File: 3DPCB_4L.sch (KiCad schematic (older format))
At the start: 196 parts, among them IC1 A5984_LP, IC2 A5984_LP, IC3 A5984_LP, IC4 A5984_LP, IC5 A5984_LP, IC6 MP9943, J10 , J11 , J12 , J13 , J14 , J15 , J16 , J5 , J6 , J7 , J8 , J9 , K1 CONN_3, K2 CONN_3, K3 CONN_3, K4 CONN_3, K5 CONN_3, K6 CONN_3, K7 CONN_3, K8 CONN_3, K9 CONN_3, P1 CONN_8, P11 CONN_3X2, P12 CONN_3X2, P13 CONN_4, P2 CONN_8, P5 CONN_4, P6 CONN_4, P7 CONN_4, P8 CONN_02X03, P9 CONN_4, U1 CONN_4_LERCHE, U10 MICRO-SD, U11 TC4427, U12 MCP4728, U13 CONN_4_LERCHE, U15 SPST_MOMENTARY, U16 CONN_4_LERCHE, U2 SPST_MOMENTARY, U21 CONN_4_LERCHE, U22 CONN_4_LERCHE, U23 MCP4728, U24 IRFH5302, U25 CONN_4_LERCHE, U3 BSS84, U4 CONN_4_LERCHE, U5 IRFH5302, U6 LPC1768_TQFP100, U7 IRFH5302, U8 IRFH5302, U9 TC4427

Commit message: Starting the work
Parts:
- removed C17: 100n, LercheTech:Lerche_C0603, symbol C-RESCUE-3DPCB_4L
- removed C9: 18p, LercheTech:Lerche_C0603, symbol C-RESCUE-3DPCB_4L
- removed D6: LED, LEDs:LED_0603, symbol LED-RESCUE-3DPCB_4L
- removed J10, J11, J12, J13, J14, J15, J16, J5, J6, J7, J8, J9: (no value), LercheTech:Lerche_2PsolderJumper, symbol SOLDER_JUMPER
- removed K8: CONN_3, Pin_Headers:Pin_Header_Straight_1x03, symbol CONN_3
- removed L1: INDUCTOR, LercheTech:Lerche_R0603, symbol INDUCTOR
- removed P11: CONN_3X2, Pin_Headers:Pin_Header_Straight_2x03, symbol CONN_3X2
- removed P12: CONN_3X2, LercheTech:Lerche_6P_1.6mm_2ROW, symbol CONN_3X2
- removed R28: 1k, LercheTech:Lerche_R0603, symbol R-RESCUE-3DPCB_4L
- removed R9: 10k, LercheTech:Lerche_R0603, symbol R-RESCUE-3DPCB_4L
- removed U10: MICRO-SD, LercheTech:Lerche_Molex_502774-0891, symbol MICRO-SD
- removed U15: SPST_MOMENTARY, LercheTech:Lerche_SPST_ITEAD, symbol SPST_MOMENTARY
- removed U16: CONN_4_LERCHE, LercheTech:Lerche_4P_2.54mm, symbol CONN_4_LERCHE
- removed U3: BSS84, LercheTech:Lerche_SOT23-3, symbol BSS84
- removed U6: LPC1768_TQFP100, Housings_QFP:TQFP-100_14x14mm_Pitch0.5mm, symbol LPC1768_TQFP100
- added C9: 1uF, LercheTech:Lerche_C0603, symbol C
- added L3, L4: L_Small, Resistors_SMD:R_0603, symbol L_Small
- added U10: MICRO-SD_Molex_502774-0891, LercheTech:Lerche_Molex_502774-0891, symbol MICRO-SD_Molex_502774-0891
- added U3: CONN_4_LERCHE, LercheTech:Lerche_4P_2.54mm, symbol CONN_4_LERCHE
- C5: value 18p -> 100n
- IC7: renamed from IC?; footprint (none) -> LercheTech:TFBGA180
- JP1, JP2: renamed from JP?; footprint (none) -> Pin_Headers:Pin_Header_Straight_1x03_Pitch2.54mm
- L5, L6, L7, L8: renamed from L?; footprint (none) -> Resistors_SMD:R_0603
- P8: footprint (none) -> LercheTech:Lerche_2x3P_3.5mm_Molex_UltraFit
- R11: value 1k5 -> 12k1 1%
- R42, R43: value 10k -> 4K7
- R44, R45: value 3k3 -> 4K7
- R7: value 33R -> 100R
- R8: value 33R -> 10k
- gave numbers to parts that had none: 5
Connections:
- net DAC_SCL is gone; now on net ISC0_SCL: R19.1, U12.2 (SCL), U23.2 (SCL)
- net DAC_SDA is gone; now on net ISC0_SDA: R18.1, U12.3 (SDA), U23.3 (SDA)
- net LED1 is gone; now on net MCU_G2_10: R3.2, U4.1
- net LED2 is gone; now on net MCU_G2_9: R4.2, U4.2
- net M1_MS1 is gone; now on net MCU_G1_13: IC1.5 (MS1)
- net P2.4 is gone; now on net MCU_PWM15: U9.2 (IN)
- net P2.5 is gone; now on net MCU_PWM14: U9.4 (IN)
- net P2.6 is gone; now on net MCU_PWM13: U11.2 (IN)
- net P2.7 is gone; now on net MCU_PWM12: U11.4 (IN)
- net PLAY is gone; now on net MCU_~ISP: R27.2
- net RX_0 is gone; now on net MCU_RXD0: K7.2 (PM)
- net SD_MOSI is gone; now on net +3.3V: R41.2
- net TH1 is gone; now on an unnamed net: C3.1, P1.2 (P2), R34.2
- net TH2 is gone; now on an unnamed net: C4.1, P1.4 (P4), R10.2
- net TH3 is gone; now on an unnamed net: C7.1, P1.6 (P6), R12.2
- net TH4 is gone; now on an unnamed net: C10.1, P1.8 (P8), R13.2
- net TX_0 is gone; now on net MCU_TXD0: K7.1 (P1)
- net USB_D- is gone; now on net USB0_VBUS: R7.2
- net X-MAX is gone; now on net MCU_G2_0: K2.3 (P3)
- net X-MIN is gone; now on net MCU_G4_0: K1.3 (P3)
- net +3.3V: now also C5.1, IC7.B9 (VBAT), IC7.D8 (VDDREG), IC7.E8 (VDDREG), IC7.G10 (VDDIO), IC7.H10 (VDDIO), IC7.H5 (VDDIO), IC7.K8 (VDDIO), R8.1, C9.1, U10.4 (+3V3); no longer IC7.B9 (VBAT), IC7.D8 (VDDREG), IC7.E8 (VDDREG), IC7.G10 (VDDIO), IC7.H10 (VDDIO), IC7.H5 (VDDIO), IC7.K8 (VDDIO), R41.1, R42.1, R43.1, R44.1, R45.1
- net ADC0/DAC: now also IC7.B6 (ADC0/DAC); no longer IC7.B6 (ADC0/DAC)
- net ADC1: now also IC7.C4 (ADC1), R42.1; no longer IC7.C4 (ADC1)
- net ADC2: now also IC7.B3 (ADC2), R43.1; no longer IC7.B3 (ADC2)
- net ADC3: now also IC7.B4 (ADC3), R44.1; no longer IC7.B4 (ADC3)
- net ADC4: now also IC7.A5 (ADC4), R45.1; no longer IC7.A5 (ADC4)
- net ADC5: now also IC7.C3 (ADC5); no longer IC7.C3 (ADC5)
- net ADC6: now also IC7.A4 (ADC6); no longer IC7.A4 (ADC6)
- net ADC7: now also IC7.B5 (ADC7); no longer IC7.B5 (ADC7)
- net DBGEN: now also IC7.K4 (DBGEN); no longer IC7.K4 (DBGEN)
- net DRV_RESET: now also IC7.H13 (P6_9)
- net FPGA_PROG: now also IC7.K1 (P8_8); no longer IC7.K1 (P8_8)
- net GND: now also IC7.D7 (VSS), IC7.E6 (VSS), IC7.E7 (VSS), IC7.E9 (VSS), IC7.F10 (VSS), IC7.K6 (VSS), IC7.K9 (VSS), R11.2, C9.2, L4.1, U10.10 (CardDetect), U10.11 (Shield), U10.12 (Shield), U10.13 (Shield), U10.14 (Shield), U10.6 (GND), U3.4; no longer IC7.D7 (VSS), IC7.E6 (VSS), IC7.E7 (VSS), IC7.E9 (VSS), IC7.F10 (VSS), IC7.K6 (VSS), IC7.K9 (VSS)
- net ISC0_SCL: now also IC7.K13 (ISC0_SCL); no longer IC7.K13 (ISC0_SCL)
- net ISC0_SDA: now also IC7.K14 (ISC0_SDA); no longer IC7.K14 (ISC0_SDA)
- net MCU_ADC6: now also IC7.C5 (PB_6); no longer IC7.C5 (PB_6)
- net MCU_BOOT0: now also IC7.N1 (P1_1); no longer IC7.N1 (P1_1)
- net MCU_BOOT1: now also IC7.N2 (P1_2); no longer IC7.N2 (P1_2)
- net MCU_BOOT2: now also IC7.H14 (P2_8); no longer IC7.H14 (P2_8)
- net MCU_BOOT3: now also IC7.G14 (P2_9); no longer IC7.G14 (P2_9)
- net MCU_G0_5: now also IC3.11 (STEP), IC7.K12 (P6_6); no longer IC7.K12 (P6_6)
- net MCU_G1_0: now also IC7.N4 (P1_7); no longer IC7.N4 (P1_7)
- net MCU_G1_1: now also IC7.M5 (P1_8); no longer IC7.M5 (P1_8)
- net MCU_G1_11: now also IC2.5 (MS1), IC7.E13 (P2_11); no longer IC7.E13 (P2_11)
- net MCU_G1_12: now also IC2.23 (~ENABLE), IC7.D13 (P2_12); no longer IC7.D13 (P2_12)
- net MCU_G1_13: now also IC7.E14 (P2_13); no longer IC7.E14 (P2_13)
- net MCU_G2_0: now also IC7.D4 (P4_0); no longer IC7.D4 (P4_0)
- net MCU_G2_10: now also IC7.M1 (P5_1); no longer IC7.M1 (P5_1)
- net MCU_G2_11: now also IC7.M3 (P5_2); no longer IC7.M3 (P5_2)
- net MCU_G2_12: now also IC7.P6 (P5_3); no longer IC7.P6 (P5_3)
- net MCU_G2_13: now also IC7.N7 (P5_4); no longer IC7.N7 (P5_4)
- net MCU_G2_14: now also IC7.N8 (P5_5); no longer IC7.N8 (P5_5)
- net MCU_G2_15: now also IC7.M11 (P5_6); no longer IC7.M11 (P5_6)
- net MCU_G2_4: now also IC7.A1 (P4_4); no longer IC7.A1 (P4_4)
- net MCU_G2_7: now also IC7.N11 (P5_7); no longer IC7.N11 (P5_7)
- net MCU_G2_9: now also IC7.L2 (P5_0); no longer IC7.L2 (P5_0)
- net MCU_G3_0: now also IC4.11 (STEP), IC7.P14 (P6_1); no longer IC7.P14 (P6_1)
- net MCU_G3_1: now also IC3.10 (MS3), IC7.K11 (P6_2); no longer IC7.K11 (P6_2)
- net MCU_G3_10: now also IC1.23 (~ENABLE), IC7.A14 (P7_2); no longer IC7.A14 (P7_2)
- net MCU_G3_2: now also IC4.6 (MS2), IC7.N13 (P6_3); no longer IC7.N13 (P6_3)
- net MCU_G3_3: now also IC4.14 (DIR), IC7.M14 (P6_4); no longer IC7.M14 (P6_4)
- net MCU_G3_4: now also IC4.10 (MS3), IC7.L14 (P6_5); no longer IC7.L14 (P6_5)
- net MCU_G3_5: no longer IC7.H13 (P6_9)
- net MCU_G3_6: now also IC2.11 (STEP), IC7.G13 (P6_10); no longer IC7.G13 (P6_10)
- net MCU_G4_0: now also IC7.E4 (P8_0); no longer IC7.E4 (P8_0)
- net MCU_G5_12: now also IC7.D2 (P4_8); no longer IC7.D2 (P4_8)
- net MCU_G5_15: now also IC2.14 (DIR), IC7.H11 (P6_7); no longer IC7.H11 (P6_7)
- net MCU_G5_6: now also IC3.6 (MS2), IC7.J14 (P2_6); no longer IC7.J14 (P2_6)
- net MCU_G6_25: now also IC7.M7 (PD_11); no longer IC7.M7 (PD_11)
- net MCU_G6_26: now also IC7.P9 (PD_12); no longer IC7.P9 (PD_12)
- net MCU_G6_28: now also IC7.L11 (PD_14); no longer IC7.L11 (PD_14)
- net MCU_G6_29: now also IC7.P13 (PD_15); no longer IC7.P13 (PD_15)
- net MCU_G6_30: now also IC7.P12 (PD_16); no longer IC7.P12 (PD_16)
- net MCU_G7_2: now also IC3.14 (DIR), IC7.L12 (PE_2); no longer IC7.L12 (PE_2)
- net MCU_G7_3: now also IC3.23 (~ENABLE), IC7.K10 (PE_3); no longer IC7.K10 (PE_3)
- net MCU_G7_4: now also IC3.5 (MS1), IC7.J11 (PE_4); no longer IC7.J11 (PE_4)
- net MCU_MISO1: now also IC7.M2 (P1_3); no longer IC7.M2 (P1_3)
- net MCU_MOSI1: now also IC7.P2 (P1_4); no longer IC7.P2 (P1_4)
- net MCU_PWM0: now also IC7.A2 (P4_2); no longer IC7.A2 (P4_2)
- net MCU_PWM1: now also IC7.D3 (P4_1); no longer IC7.D3 (P4_1)
- net MCU_PWM10: now also IC7.D14 (PB_0); no longer IC7.D14 (PB_0)
- net MCU_PWM11: now also IC7.F5 (P7_6); no longer IC7.F5 (P7_6)
- net MCU_PWM12: now also IC7.A7 (P7_5); no longer IC7.A7 (P7_5)
- net MCU_PWM13: now also IC7.C6 (P7_4); no longer IC7.C6 (P7_4)
- net MCU_PWM14: now also IC7.B14 (P7_0); no longer IC7.B14 (P7_0)
- net MCU_PWM15: now also IC7.C13 (P7_1); no longer IC7.C13 (P7_1)
- net MCU_PWM2: now also IC7.F14 (P2_10); no longer IC7.F14 (P2_10)
- net MCU_PWM3: now also IC7.B2 (P4_3); no longer IC7.B2 (P4_3)
- net MCU_PWM4: now also IC7.B1 (P4_6); no longer IC7.B1 (P4_6)
- net MCU_PWM5: now also IC7.C2 (P4_5); no longer IC7.C2 (P4_5)
- net MCU_PWM6: now also IC7.A13 (PB_1); no longer IC7.A13 (PB_1)
- net MCU_PWM7: now also IC7.B11 (PB_2); no longer IC7.B11 (PB_2)
- net MCU_PWM8: now also IC7.A12 (PB_3); no longer IC7.A12 (PB_3)
- net MCU_PWM9: now also IC7.E12 (PA_4); no longer IC7.E12 (PA_4)
- net MCU_RD0: now also IC7.D10 (P3_1); no longer IC7.D10 (P3_1)
- net MCU_RD1: now also IC7.M12 (PE_1); no longer IC7.M12 (PE_1)
- net MCU_RXD0: now also IC7.M13 (P2_1); no longer IC7.M13 (P2_1)
- net MCU_RXD1: now also IC7.K7 (P1_14); no longer IC7.K7 (P1_14)
- net MCU_RXD2: now also IC7.J13 (PA_2); no longer IC7.J13 (PA_2)
- net MCU_RXD3: now also IC7.L9 (P2_4); no longer IC7.L9 (P2_4)
- net MCU_SCK0: now also IC7.D12 (P3_0); no longer IC7.D12 (P3_0)
- net MCU_SCK1: now also IC7.D6 (PF_4); no longer IC7.D6 (PF_4)
- net MCU_SGPIO0: now also IC7.P1 (P9_0); no longer IC7.P1 (P9_0)
- net MCU_SGPIO15: now also IC7.L3 (P4_10); no longer IC7.L3 (P4_10)
- net MCU_SSEL1: now also IC7.N3 (P1_5); no longer IC7.N3 (P1_5)
- net MCU_TD0: now also IC7.D9 (P3_2); no longer IC7.D9 (P3_2)
- net MCU_TD1: now also IC7.N12 (PE_0); no longer IC7.N12 (PE_0)
- net MCU_TXD0: now also IC7.N14 (P2_0); no longer IC7.N14 (P2_0)
- net MCU_TXD2: now also IC7.H12 (PA_1); no longer IC7.H12 (PA_1)
- net MCU_TXD3: now also IC7.G11 (P2_3); no longer IC7.G11 (P2_3)
- net MCU_~DFU: now also IC7.J2 (P4_9), R8.2, U3.1; no longer IC7.J2 (P4_9)
- net MCU_~ISP: now also IC7.G12 (P2_7), U3.2; no longer IC7.G12 (P2_7)
- net NC_CGU1: now also IC7.L10 (PA_0); no longer IC7.L10 (PA_0)
- net NC_ETH_CRS: now also IC7.L5 (P1_16); no longer IC7.L5 (P1_16)
- net NC_ETH_LED1: now also IC7.L1 (P1_0); no longer IC7.L1 (P1_0)
- net NC_ETH_MDC: now also IC7.D5 (P7_7); no longer IC7.D5 (P7_7)
- net NC_ETH_MDIO: now also IC7.L6 (P1_17); no longer IC7.L6 (P1_17)
- net NC_ETH_REF_CLK: now also IC7.N9 (P1_19); no longer IC7.N9 (P1_19)
- net NC_ETH_RXD0: now also IC7.P11 (P1_15); no longer IC7.P11 (P1_15)
- net NC_ETH_RXD1: now also IC7.K3 (P0_0); no longer IC7.K3 (P0_0)
- net NC_ETH_TXD0: now also IC7.N10 (P1_18); no longer IC7.N10 (P1_18)
- net NC_ETH_TXD1: now also IC7.J10 (P1_20); no longer IC7.J10 (P1_20)
- net NC_ETH_TXEN: now also IC7.K2 (P0_1); no longer IC7.K2 (P0_1)
- net NC_MCU_G2_8: now also IC7.F13 (P6_12); no longer IC7.F13 (P6_12)
- net NC_MCU_G3_11: now also IC7.C12 (P7_3); no longer IC7.C12 (P7_3)
- net NC_MCU_G3_7: now also IC7.F11 (P6_11); no longer IC7.F11 (P6_11)
- net NC_MCU_G4_1: now also IC7.G4 (P8_1); no longer IC7.G4 (P8_1)
- net NC_MCU_G4_10: now also IC7.E10 (PA_3); no longer IC7.E10 (PA_3)
- net NC_MCU_G4_2: now also IC7.J4 (P8_2); no longer IC7.J4 (P8_2)
- net NC_MCU_G4_3: now also IC7.H3 (P8_3); no longer IC7.H3 (P8_3)
- net NC_MCU_G4_4: now also IC7.H2 (P8_4); no longer IC7.H2 (P8_4)
- net NC_MCU_G4_5: now also IC7.H1 (P8_5); no longer IC7.H1 (P8_5)
- net NC_MCU_G4_6: now also IC7.J3 (P8_6); no longer IC7.J3 (P8_6)
- net NC_MCU_G4_7: now also IC7.J1 (P8_7); no longer IC7.J1 (P8_7)
- net NC_MCU_G5_16: now also IC7.F12 (P6_8); no longer IC7.F12 (P6_8)
- net NC_MCU_G5_24: now also IC7.B10 (PB_4); no longer IC7.B10 (PB_4)
- net NC_MCU_G5_25: now also IC7.A11 (PB_5); no longer IC7.A11 (PB_5)
- net NC_MCU_SGPIO1: now also IC7.P4 (P9_1); no longer IC7.P4 (P9_1)
- net NC_MCU_SGPIO2: now also IC7.M6 (P9_2); no longer IC7.M6 (P9_2)
- net NC_P4_7: now also IC7.F4 (P4_7); no longer IC7.F4 (P4_7)
- net NC_P6_0: now also IC7.M10 (P6_0); no longer IC7.M10 (P6_0)
- net NC_USB0_LED0: now also IC7.J12 (P2_5); no longer IC7.J12 (P2_5)
- net NC_USB0_LED1: now also IC7.L13 (P2_2); no longer IC7.L13 (P2_2)
- net NC_USB1_LED0: now also IC7.M8 (P9_4); no longer IC7.M8 (P9_4)
- net NC_USB1_LED1: now also IC7.P5 (P9_3); no longer IC7.P5 (P9_3)
- net SD_CMD: now also IC7.P3 (P1_6), U10.3 (CMD/MOSI); no longer IC7.P3 (P1_6)
- net SD_DAT0: now also IC7.N5 (P1_9), U10.7 (DAT0/MISO); no longer IC7.N5 (P1_9)
- net SD_DAT1: now also IC7.N6 (P1_10), U10.8 (DAT1/x); no longer IC7.N6 (P1_10)
- net SD_DAT2: now also IC7.P8 (P1_11), U10.1 (DAT2/x); no longer IC7.P8 (P1_11)
- net SD_DAT3: now also IC7.P7 (P1_12), U10.2 (DAT3/~CS); no longer IC7.P7 (P1_12)
- net SPIFI_CS: now also IC7.C9 (P3_8); no longer IC7.C9 (P3_8)
- net SPIFI_SCK: now also IC7.B13 (P3_3); no longer IC7.B13 (P3_3)
- net SPIFI_SIO0: now also IC7.C10 (P3_7); no longer IC7.C10 (P3_7)
- net SPIFI_SIO1: now also IC7.B12 (P3_6); no longer IC7.B12 (P3_6)
- net SPIFI_SIO2: now also IC7.C11 (P3_5); no longer IC7.C11 (P3_5)
- net SPIFI_SIO3: now also IC7.C14 (P3_4); no longer IC7.C14 (P3_4)
- net TCK/SWDCLK: now also IC7.G5 (TCK/SWDCLK); no longer IC7.G5 (TCK/SWDCLK)
- net TDI: now also IC7.H4 (TDI); no longer IC7.H4 (TDI)
- net TDO/SWO: now also IC7.J5 (TDO/SWO); no longer IC7.J5 (TDO/SWO)
- net TMS/SWDIO: now also IC7.K5 (TMS/SWDIO); no longer IC7.K5 (TMS/SWDIO)
- net USB0_D+: now also CONN1.3 (D+), IC7.E2 (USB0_DP); no longer IC7.E2 (USB0_DP)
- net USB0_D-: now also CONN1.2 (D-), IC7.F2 (USB0_DM); no longer IC7.F2 (USB0_DM)
- net USB0_VBUS: now also IC7.E1 (USB0_VBUS); no longer IC7.E1 (USB0_VBUS)
- net USB1_D+: now also IC7.D11 (USB1_DP); no longer IC7.D11 (USB1_DP)
- net USB1_D-: now also IC7.E11 (USB1_DM); no longer IC7.E11 (USB1_DM)
- net USB1_PPWR: now also IC7.L7 (P9_5); no longer IC7.L7 (P9_5)
- net USB1_PWR_FLT: now also IC7.M9 (P9_6); no longer IC7.M9 (P9_6)
- net USB_RREF: now also IC7.G1 (USB0_RREF), R11.1; no longer IC7.G1 (USB0_RREF)
- net ~RESET: now also IC7.C7 (~RESET), U3.3; no longer IC7.C7 (~RESET)
- net ~TRST: now also IC7.L4 (~TRST~); no longer IC7.L4 (~TRST~)
- net at CONN1.1 (+5V): now also L3.1; no longer D5.1 (A)
- net at R7.1: now also D5.1 (A), L3.2; no longer CONN1.2 (D-)
- net at CONN1.4 (ID): now also L4.2
- net at C18.2: now also IC7.C1 (XTAL1); no longer IC7.C1 (XTAL1)
- net MCU_G7_7: now reaches IC2.6 (MS2)
- net MCU_G2_8: now reaches IC2.10 (MS3)
- net MCU_G7_5: now reaches IC4.5 (MS1)
- net at L6.1: now also IC7.A3 (VSSA); no longer IC7.A3 (VSSA)
- net at L5.2: now also IC7.A6 (VDDA); no longer IC7.A6 (VDDA)
- net DIR1: no longer names the net of U1.2
- net DIR1: no longer IC1.14 (DIR)
- net DIR2: no longer names the net of U21.2
- net DIR2: no longer IC2.14 (DIR)
- net DIR3: no longer names the net of U22.2
- net DIR3: no longer IC3.14 (DIR)
- net DIR4: no longer names the net of U25.2
- net DIR4: no longer IC4.14 (DIR)
- net DIR5: no longer names the net of U13.2
- net DIR5: no longer IC5.14 (DIR)
- net EN1: no longer names the net of U1.3
- net EN1: no longer IC1.23 (~ENABLE)
- net EN2: no longer names the net of U21.3
- net EN2: no longer IC2.23 (~ENABLE)
- net EN3: no longer names the net of U22.3
- net EN3: no longer IC3.23 (~ENABLE)
- net EN4: no longer names the net of U25.3
- net EN4: no longer IC4.23 (~ENABLE)
- net EN5: no longer names the net of U13.3
- net EN5: no longer IC5.23 (~ENABLE)
- net LED3 renamed MCU_G6_13
- net LED4 renamed MCU_G6_12
- net M1_MS2 renamed MCU_G7_14
- net M1_MS3 renamed MCU_G7_11
- removed net MCU_TXD1: IC7.L8 (P1_13)
- net SCL: no longer names the net of R45.2
- net SDA: no longer names the net of R44.2
- net SD_CS: no longer names the net of R43.2
- net SD_MISO: no longer names the net of R42.2
- net STP1: no longer names the net of U1.1
- net STP1: no longer IC1.11 (STEP)
- net STP2: no longer names the net of U21.1
- net STP2: no longer IC2.11 (STEP)
- net STP3: no longer names the net of U22.1
- net STP3: no longer IC3.11 (STEP)
- net STP4: no longer names the net of U25.1
- net STP4: no longer IC4.11 (STEP)
- net STP5: no longer names the net of U13.1
- net STP5: no longer IC5.11 (STEP)
- removed net USB_D+: C5.1, R11.2, R8.2
- net Y-MIN renamed MCU_G7_22
- new net: IC7.E3 (USB0_VDDA), IC7.F3 (USB0_VDDA3V3), L7.2
- new net: IC7.F1 (USB0_VSSA), IC7.G3 (USB0_VSSA), L8.1
- new net MCU_G7_12: IC1.11 (STEP)
- new net MCU_G7_6: IC4.23 (~ENABLE)
- new net MCU_G7_9: IC1.14 (DIR)
- new net SD_CD: IC7.L8 (P1_13), R41.1, U10.9 (CardDetect)
- new net SD_CLK: IC7.M4 (CLK0), U10.5 (CLK/SCLK)
- no-connect marks 22 -> 12
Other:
- note removed: "I2C connection"
- note removed: "SPI pinout"
- note removed: "SPI_SD pinout"
- note removed: "Todo: Change so external Ethernet-board is \npossible to add. 18-11-2016"
- moved on the sheet: C12, C13, C14, C15, C16, D5, P1, R10, R11, R12, R13, R34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

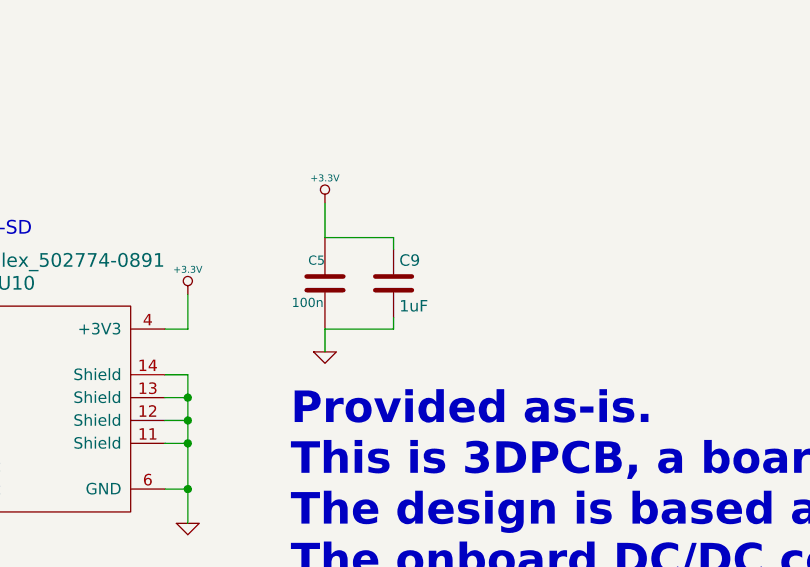
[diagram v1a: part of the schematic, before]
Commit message: TEsting routing
Testing routing options, like differential, length matching and so on.
Is not routed yet.
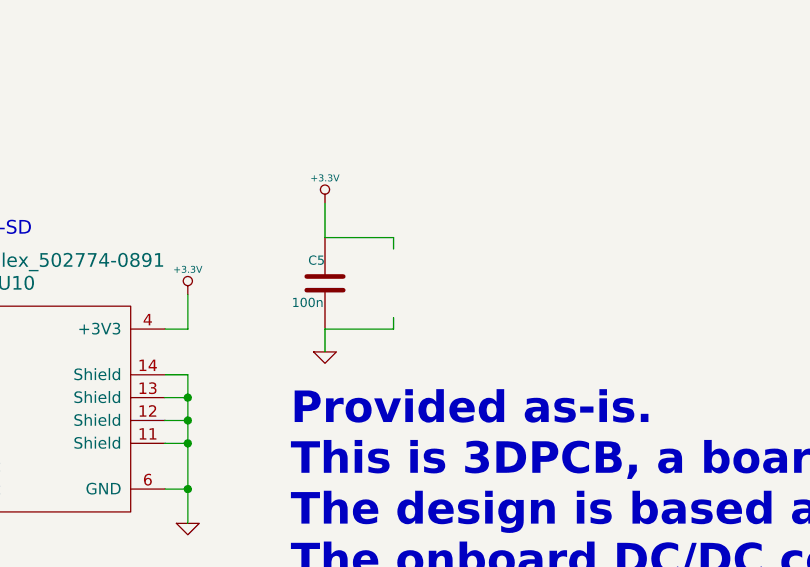
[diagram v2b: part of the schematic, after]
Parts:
- removed C9: 1uF, LercheTech:Lerche_C0603, symbol C
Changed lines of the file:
@@
-$EndComp
-$Comp
-L C C9
-U 1 1 58A42175
-P 5550 13800
-F 0 "C9" H 5575 13900 50  0000 L CNN
-F 1 "1uF" H 5575 13700 50  0000 L CNN
-F 2 "LercheTech:Lerche_C0603" H 5588 13650 50  0001 C CNN
-F 3 "" H 5550 13800 50  0000 C CNN
-	1    5550 13800
-	1    0    0    -1
 $EndComp
 $Comp
